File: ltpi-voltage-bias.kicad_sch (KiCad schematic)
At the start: 18 parts

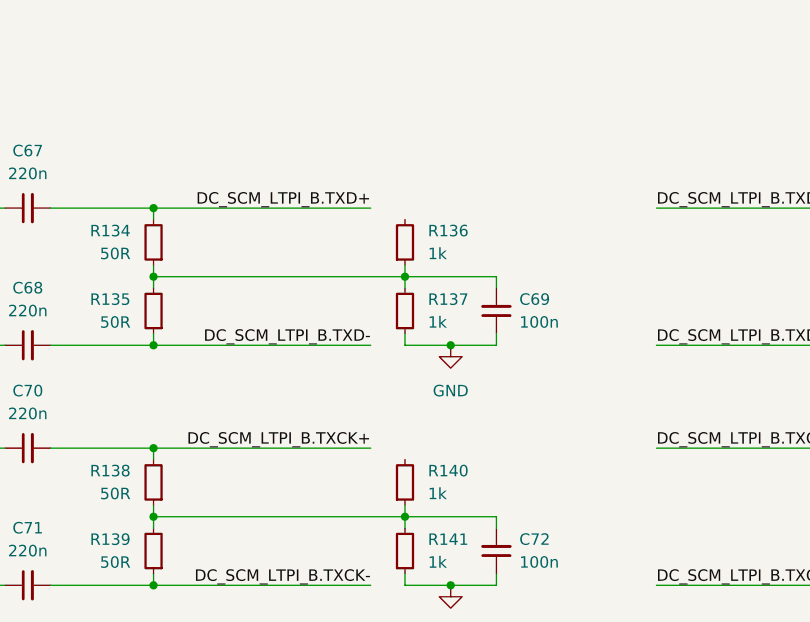
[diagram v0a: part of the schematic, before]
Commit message: [#83146] Set LTPI bias voltage
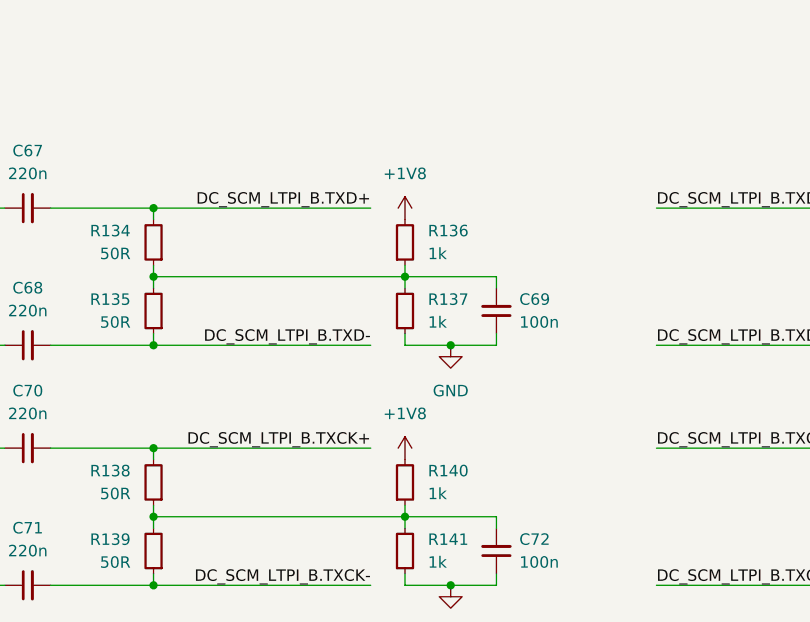
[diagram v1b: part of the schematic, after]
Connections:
- net +1V8: now reaches R140.2
- net +1V8: now also R136.2
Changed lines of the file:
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@@
+	)
+	(symbol
+		(lib_id "antmicropower:+1V8")
+		(at 158.75 58.42 0)
+		(unit 1)
+		(exclude_from_sim no)
+		(in_bom yes)
+		(on_board yes)
+		(dnp no)
+		(fields_autoplaced yes)
+		(property "Reference" "#PWR0132"
+			(at 173.99 60.96 0)
+			(effects
+				(font
+					(size 1.27 1.27)
+					(thickness 0.15)
+				)
+				(justify left bottom)
+				(hide yes)
+			)
+		)
+		(property "Value" "+1V8"
+			(at 158.75 53.34 0)
+			(effects
+				(font
+					(size 1.27 1.27)
+					(thickness 0.15)
+				)
+			)
+		)
+		(property "Footprint" ""
+			(at 173.99 66.04 0)
+			(effects
+				(font
+					(size 1.27 1.27)
+					(thickness 0.15)
+				)
+				(justify left bottom)
+				(hide yes)
+			)
+		)
+		(property "Datasheet" ""
+			(at 173.99 68.58 0)
+			(effects
+				(font
+					(size 1.27 1.27)
+					(thickness 0.15)
+				)
+				(justify left bottom)
+				(hide yes)
+			)
+		)
+		(property "Description" ""
+			(at 158.75 58.42 0)
+			(effects
+				(font
+					(size 1.27 1.27)
+				)
+				(hide yes)
+			)
+		)
+		(property "Author" "Antmicro"
+			(at 173.99 63.5 0)
+			(effects
+				(font
+					(size 1.27 1.27)
+					(thickness 0.15)
+				)
+				(justify left bottom)
+				(hide yes)
+			)
+		)
+		(property "License" "Apache-2.0"
+			(at 173.99 66.04 0)
+			(effects
+				(font
+					(size 1.27 1.27)
+					(thickness 0.15)
+				)
+				(justify left bottom)
+				(hide yes)
+			)
+		)
+		(pin "1"
+		)
+		(instances
+			(project ""
+				(path "/5f636c45-3c15-4731-8931-4625e0dab7e4/5ae3d11e-bdb2-474c-9920-031cf5845646"
+					(reference "#PWR0132")
+					(unit 1)
+				)
+			)
+		)
 	)
 	(symbol
@@
 					(unit 1)
 				)
+			)
+		)
+	)
+	(symbol
+		(lib_id "antmicropower:+1V8")
+		(at 158.75 85.09 0)
+		(unit 1)
+		(exclude_from_sim no)
+		(in_bom yes)
+		(on_board yes)
+		(dnp no)
+		(fields_autoplaced yes)
+		(property "Reference" "#PWR0133"
+			(at 173.99 87.63 0)
+			(effects
+				(font
+					(size 1.27 1.27)
+					(thickness 0.15)
+				)
+				(justify left bottom)
+				(hide yes)
+			)
+		)
+		(property "Value" "+1V8"
+			(at 158.75 80.01 0)
+			(effects
+				(font
+					(size 1.27 1.27)
+					(thickness 0.15)
+				)
+			)
+		)
+		(property "Footprint" ""
+			(at 173.99 92.71 0)
+			(effects
+				(font
+					(size 1.27 1.27)
+					(thickness 0.15)
+				)
+				(justify left bottom)
+				(hide yes)
+			)
+		)
+		(property "Datasheet" ""
+			(at 173.99 95.25 0)
+			(effects
+				(font
+					(size 1.27 1.27)
+					(thickness 0.15)
+				)
+				(justify left bottom)
+				(hide yes)
+			)
+		)
+		(property "Description" ""
+			(at 158.75 85.09 0)
+			(effects
+				(font
+					(size 1.27 1.27)
+				)
+				(hide yes)
+			)
+		)
+		(property "Author" "Antmicro"
+			(at 173.99 90.17 0)
+			(effects
+				(font
+					(size 1.27 1.27)
+					(thickness 0.15)
+				)
+				(justify left bottom)
+				(hide yes)
+			)
+		)
+		(property "License" "Apache-2.0"
+			(at 173.99 92.71 0)
+			(effects
+				(font
+					(size 1.27 1.27)
+					(thickness 0.15)
+				)
+				(justify left bottom)
+				(hide yes)
+			)
+		)
+		(pin "1"
+		)
+		(instances
+			(project "bmc-reference-carrier-board"
+				(path "/5f636c45-3c15-4731-8931-4625e0dab7e4/5ae3d11e-bdb2-474c-9920-031cf5845646"
+					(reference "#PWR0133")
+					(unit 1)
+				)

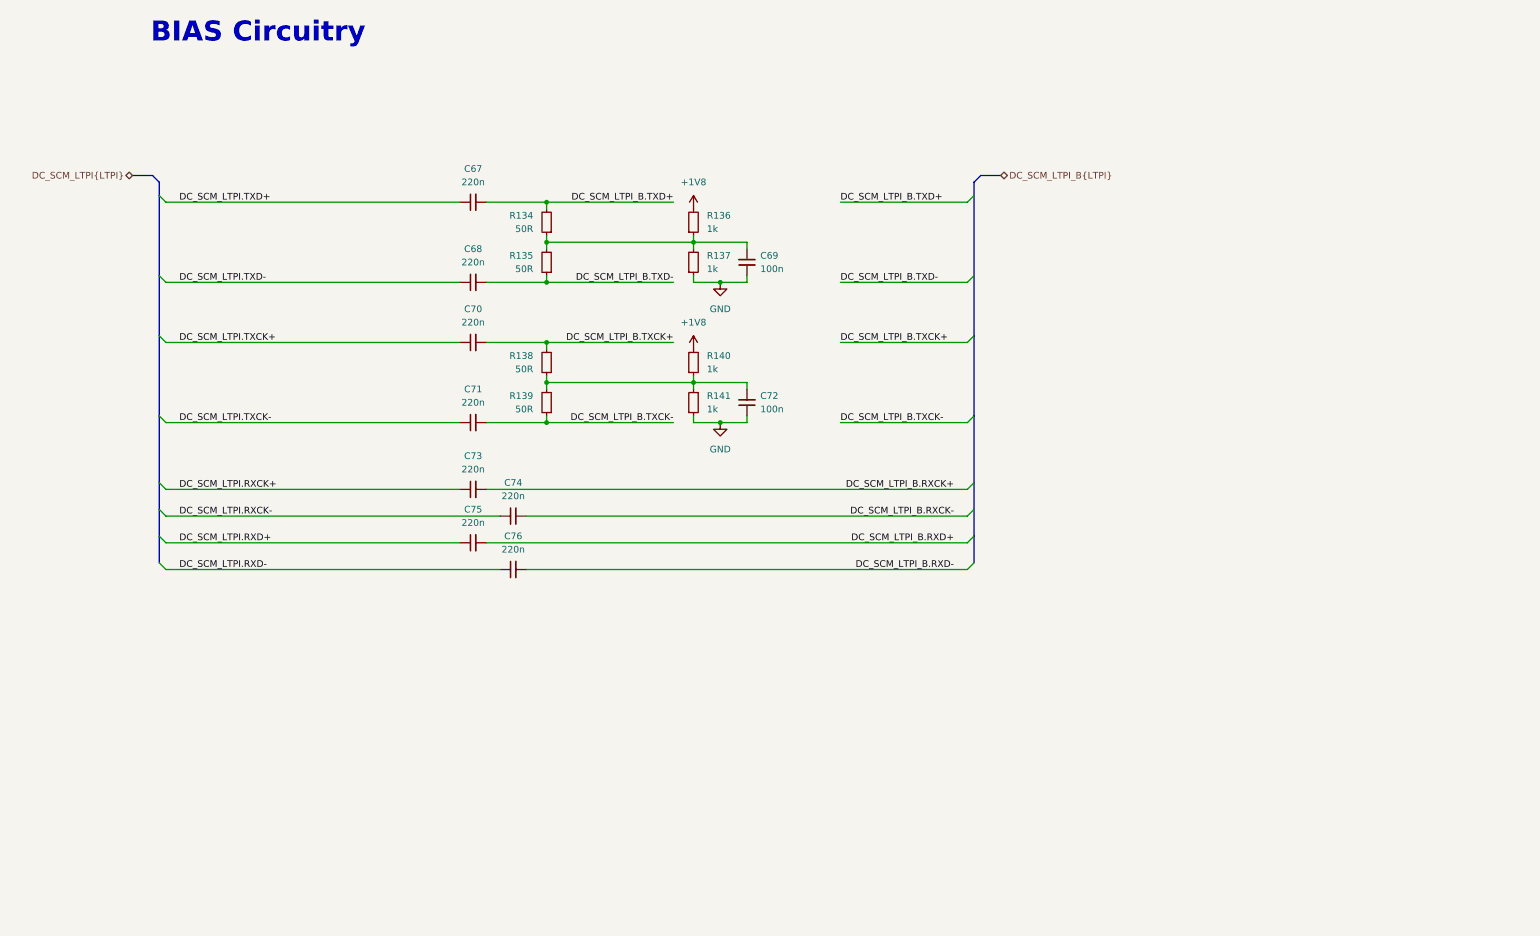
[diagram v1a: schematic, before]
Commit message: Changed A4 sheets to A3 and cleaned them up
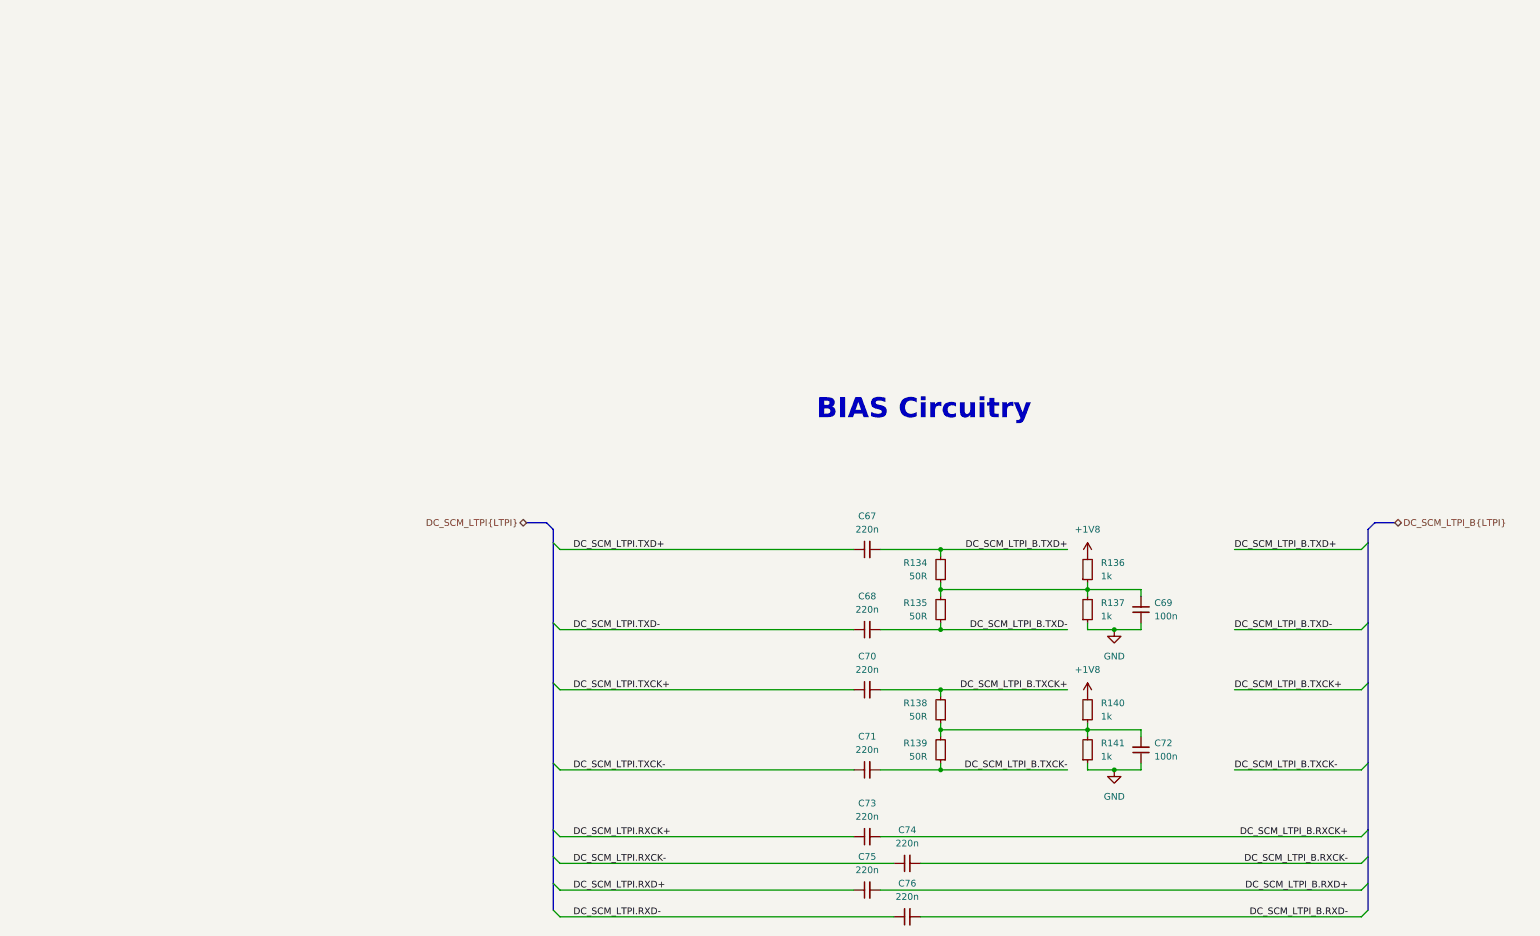
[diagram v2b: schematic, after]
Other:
- moved on the sheet: C67, C68, C69, C70, C71, C72, C73, C74, C75, C76, R134, R135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

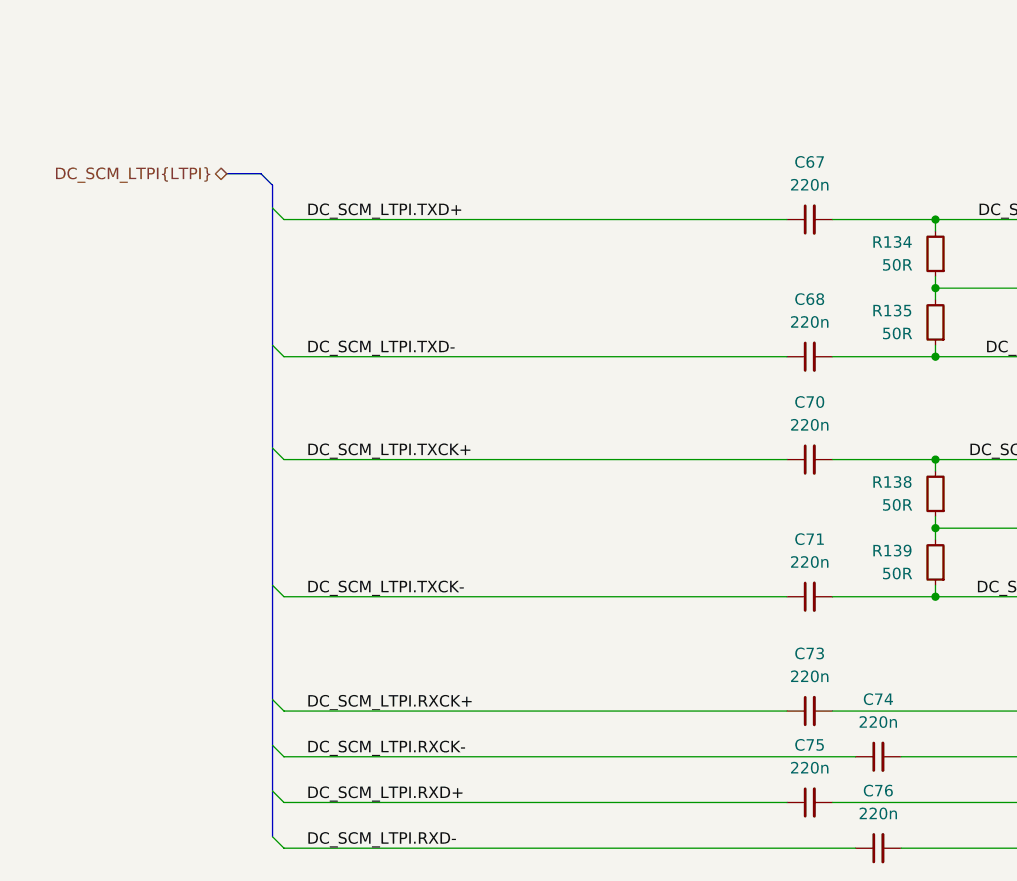
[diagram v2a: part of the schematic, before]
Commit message: [#83362] Fix connections of headers, add I2C mux
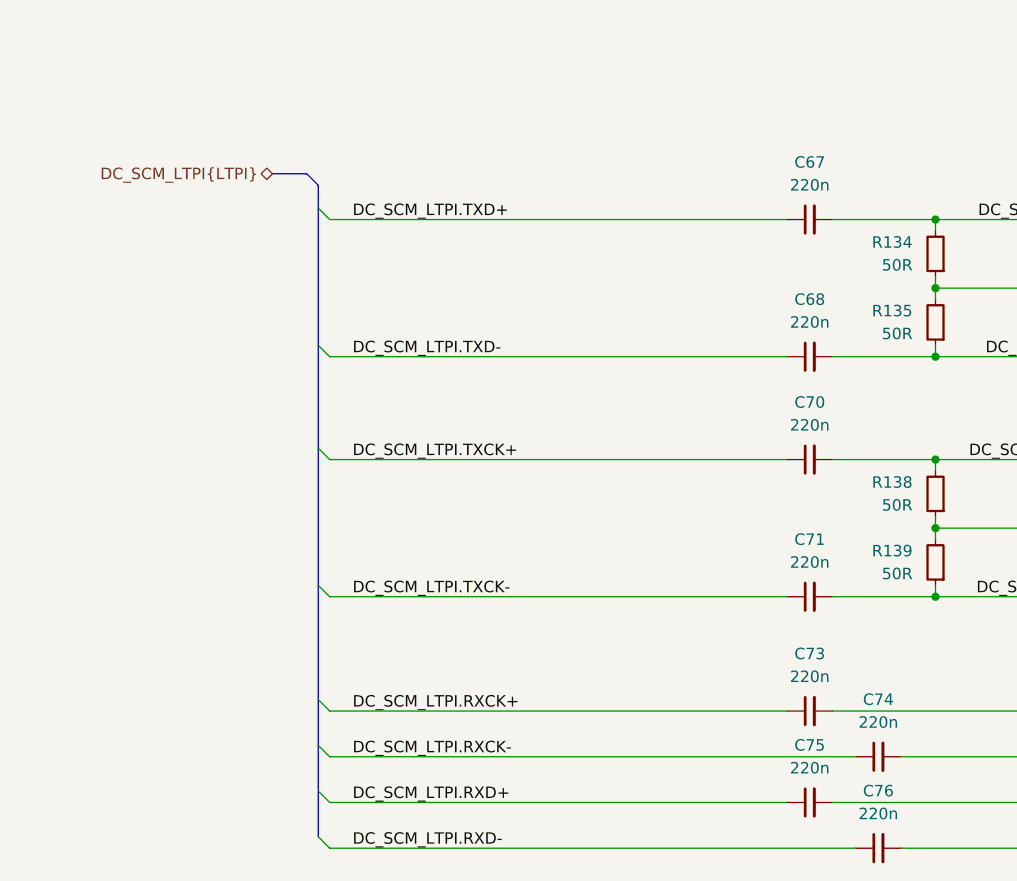
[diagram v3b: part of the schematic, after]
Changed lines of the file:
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@@
 	)
 	(bus_entry
-		(at 132.08 181.61)
+		(at 137.16 181.61)
 		(size 1.27 1.27)
 		(stroke
@@
 	)
 	(bus_entry
-		(at 132.08 176.53)
+		(at 137.16 176.53)
 		(size 1.27 1.27)
 		(stroke
@@
 	)
 	(bus_entry
-		(at 132.08 186.69)
+		(at 137.16 186.69)
 		(size 1.27 1.27)
 		(stroke
@@
 	)
 	(bus_entry
-		(at 132.08 121.92)
+		(at 137.16 121.92)
 		(size 1.27 1.27)
 		(stroke
@@
 	)
 	(bus_entry
-		(at 132.08 148.59)
+		(at 137.16 148.59)
 		(size 1.27 1.27)
 		(stroke
@@
 	)
 	(bus_entry
-		(at 132.08 137.16)
+		(at 137.16 137.16)
 		(size 1.27 1.27)
 		(stroke
@@
 	)
 	(bus_entry
-		(at 132.08 163.83)
+		(at 137.16 163.83)
 		(size 1.27 1.27)
 		(stroke
@@
 	)
 	(bus_entry
-		(at 132.08 191.77)
+		(at 137.16 191.77)
 		(size 1.27 1.27)
 		(stroke
@@
 	(wire
 		(pts
-			(xy 133.35 149.86) (xy 189.23 149.86)
+			(xy 138.43 149.86) (xy 189.23 149.86)
 		)
 		(stroke
@@
 	(wire
 		(pts
-			(xy 133.35 177.8) (xy 189.23 177.8)
+			(xy 138.43 177.8) (xy 189.23 177.8)
 		)
 		(stroke
@@
 	(wire
 		(pts
-			(xy 133.35 123.19) (xy 189.23 123.19)
+			(xy 138.43 123.19) (xy 189.23 123.19)
 		)
 		(stroke
@@
 	(bus
 		(pts
-			(xy 132.08 163.83) (xy 132.08 176.53)
+			(xy 137.16 163.83) (xy 137.16 176.53)
 		)
 		(stroke
@@
 	(wire
 		(pts
-			(xy 133.35 165.1) (xy 189.23 165.1)
-		)
-		(stroke
-			(width 0)
-			(type default)
-		)
-	)
-	(bus
-		(pts
-			(xy 132.08 181.61) (xy 132.08 186.69)
+			(xy 138.43 165.1) (xy 189.23 165.1)
+		)
+		(stroke
+			(width 0)
+			(type default)
+		)
+	)
+	(bus
+		(pts
+			(xy 137.16 181.61) (xy 137.16 186.69)
 		)
 		(stroke
@@
 	(wire
 		(pts
-			(xy 133.35 138.43) (xy 189.23 138.43)
-		)
-		(stroke
-			(width 0)
-			(type default)
-		)
-	)
-	(bus
-		(pts
-			(xy 132.08 186.69) (xy 132.08 191.77)
+			(xy 138.43 138.43) (xy 189.23 138.43)
+		)
+		(stroke
+			(width 0)
+			(type default)
+		)
+	)
+	(bus
+		(pts
+			(xy 137.16 186.69) (xy 137.16 191.77)
 		)
 		(stroke
@@
 	(bus
 		(pts
-			(xy 127 118.11) (xy 130.81 118.11)
+			(xy 132.08 118.11) (xy 135.89 118.11)
 		)
 		(stroke
@@
 	(bus
 		(pts
-			(xy 132.08 119.38) (xy 132.08 121.92)
+			(xy 137.16 119.38) (xy 137.16 121.92)
 		)
 		(stroke
@@
 	(wire
 		(pts
-			(xy 133.35 182.88) (xy 196.85 182.88)
+			(xy 138.43 182.88) (xy 196.85 182.88)
 		)
 		(stroke
@@
 	(bus
 		(pts
-			(xy 132.08 176.53) (xy 132.08 181.61)
+			(xy 137.16 176.53) (xy 137.16 181.61)
 		)
 		(stroke
@@
 	(bus
 		(pts
-			(xy 132.08 163.83) (xy 132.08 148.59)
+			(xy 137.16 163.83) (xy 137.16 148.59)
 		)
 		(stroke
@@
 	(wire
 		(pts
-			(xy 133.35 187.96) (xy 189.23 187.96)
+			(xy 138.43 187.96) (xy 189.23 187.96)
 		)
 		(stroke
@@
 	(bus
 		(pts
-			(xy 130.81 118.11) (xy 132.08 119.38)
+			(xy 135.89 118.11) (xy 137.16 119.38)
 		)
 		(stroke
@@
 	(bus
 		(pts
-			(xy 132.08 121.92) (xy 132.08 137.16)
+			(xy 137.16 121.92) (xy 137.16 137.16)
 		)
 		(stroke
@@
 	(wire
 		(pts
-			(xy 133.35 193.04) (xy 196.85 193.04)
+			(xy 138.43 193.04) (xy 196.85 193.04)
 		)
 		(stroke
@@
 	(bus
 		(pts
-			(xy 132.08 148.59) (xy 132.08 137.16)
+			(xy 137.16 148.59) (xy 137.16 137.16)
 		)
 		(stroke
@@
 	)
 	(label "DC_SCM_LTPI.TXCK-"
-		(at 135.89 165.1 0)
+		(at 140.97 165.1 0)
 		(effects
 			(font
@@
 	)
 	(label "DC_SCM_LTPI.RXD+"
-		(at 135.89 187.96 0)
+		(at 140.97 187.96 0)
 		(effects
 			(font
@@
 	)
 	(label "DC_SCM_LTPI.TXCK+"
-		(at 135.89 149.86 0)
+		(at 140.97 149.86 0)
 		(effects
 			(font
@@
 	)
 	(label "DC_SCM_LTPI.RXCK-"
-		(at 135.89 182.88 0)
+		(at 140.97 182.88 0)
 		(effects
 			(font
@@
 	)
 	(label "DC_SCM_LTPI.TXD-"
-		(at 135.89 138.43 0)
+		(at 140.97 138.43 0)
 		(effects
 			(font
@@
 	)
 	(label "DC_SCM_LTPI.RXD-"
-		(at 135.89 193.04 0)
+		(at 140.97 193.04 0)
 		(effects
 			(font
@@
 	)
 	(label "DC_SCM_LTPI.RXCK+"
-		(at 135.89 177.8 0)
+		(at 140.97 177.8 0)
 		(effects
 			(font
@@
 	)
 	(label "DC_SCM_LTPI.TXD+"
-		(at 135.89 123.19 0)
+		(at 140.97 123.19 0)
 		(effects
 			(font
@@
 	(hierarchical_label "DC_SCM_LTPI{LTPI}"
 		(shape bidirectional)
-		(at 127 118.11 180)
-		(effects
-			(font
+		(at 132.08 118.11 180)
+		(effects
+			(font
